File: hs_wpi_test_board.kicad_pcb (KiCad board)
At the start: 2 copper layers, 57.2 x 52.1 mm, 34 parts, among them J1 Raspberry_Pi_2_3, Q1 Q_NPN_EBC, Q10 Q_NPN_EBC, Q2 Q_NPN_EBC, Q3 Q_NPN_EBC, Q4 Q_NPN_EBC, Q5 Q_NPN_EBC, Q6 Q_NPN_EBC, Q7 Q_NPN_EBC, Q8 Q_NPN_EBC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

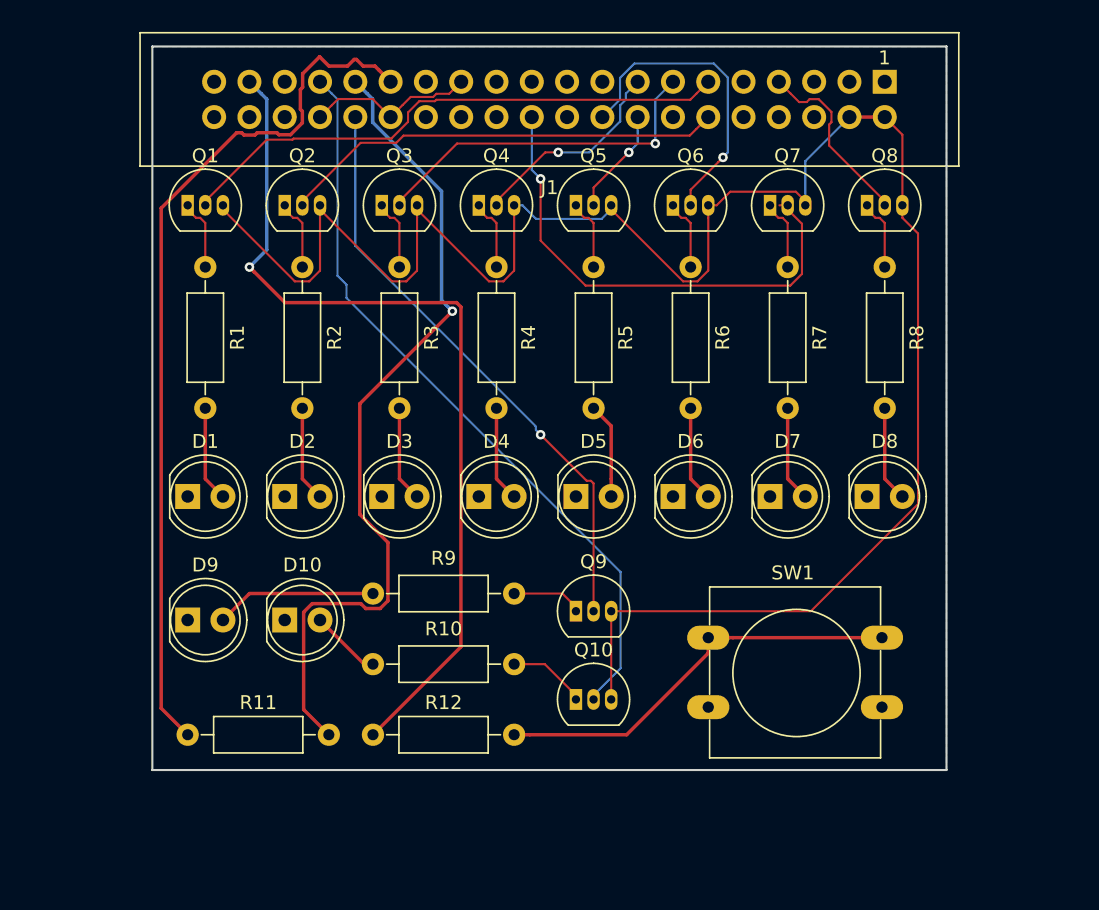
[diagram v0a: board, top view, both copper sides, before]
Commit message: remove all routing
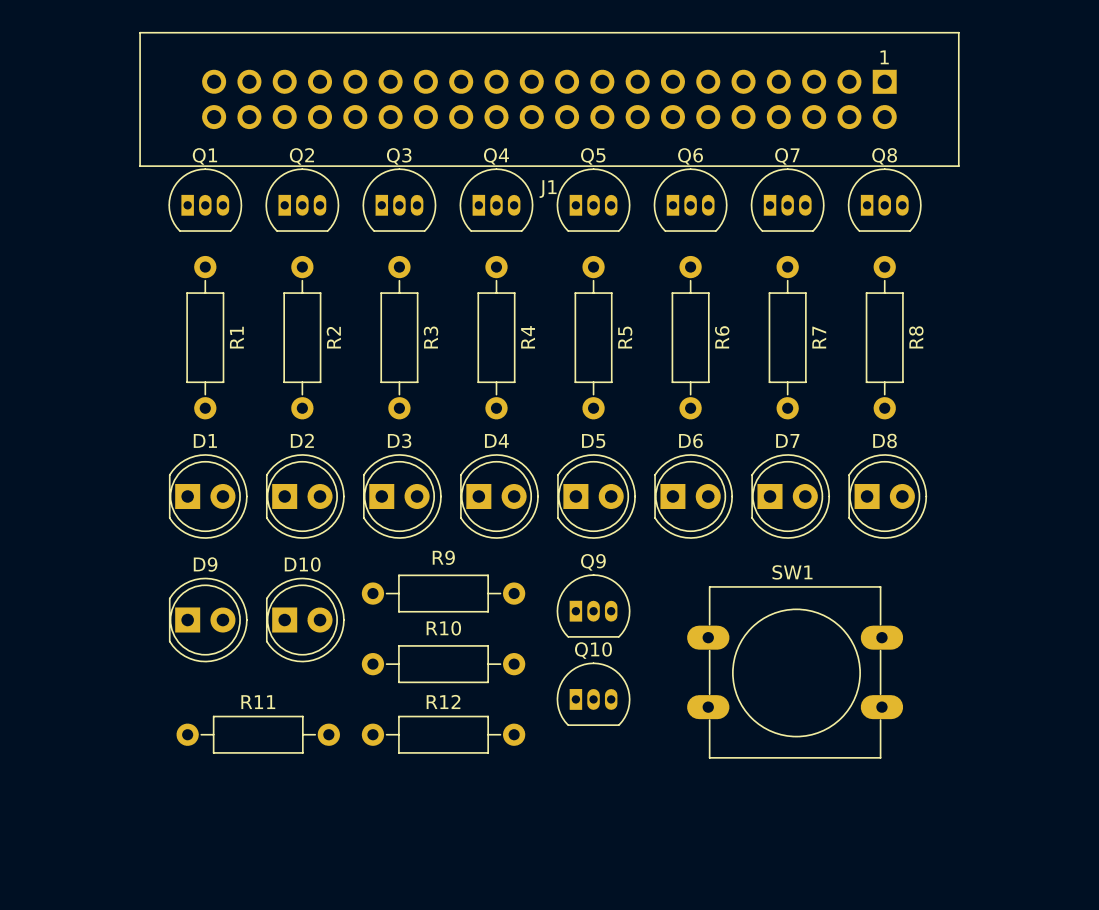
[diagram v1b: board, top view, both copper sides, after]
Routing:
- net VCC: track 144.4 -> 0.00 mm
- net /Button: track 64.2 -> 0.00 mm, vias 1 -> 0
- net Net-(J1-Pad29): track 63.3 -> 0.00 mm
- net Net-(J1-Pad31): track 60.1 -> 0.00 mm, vias 1 -> 0
- net /PWM1: track 54.2 -> 0.00 mm
- net /PWM0: track 42.8 -> 0.00 mm, vias 1 -> 0
- net /WPi0: track 40.4 -> 0.00 mm
- net /WPi6: track 35.6 -> 0.00 mm, vias 1 -> 0
- net /WPi1: track 32.0 -> 0.00 mm
- net Net-(R12-Pad2): track 30.0 -> 0.00 mm
- net /WPi2: track 25.4 -> 0.00 mm, vias 1 -> 0
- net /WPi5: track 22.2 -> 0.00 mm, vias 1 -> 0
- net /WPi3: track 15.0 -> 0.00 mm, vias 1 -> 0
- net /WPi7: track 13.3 -> 0.00 mm
- net GND: track 12.3 -> 0.00 mm
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- removed copper zone on B.Cu, net GND
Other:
- board outline removed

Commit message: switch to wider footprint for transistors
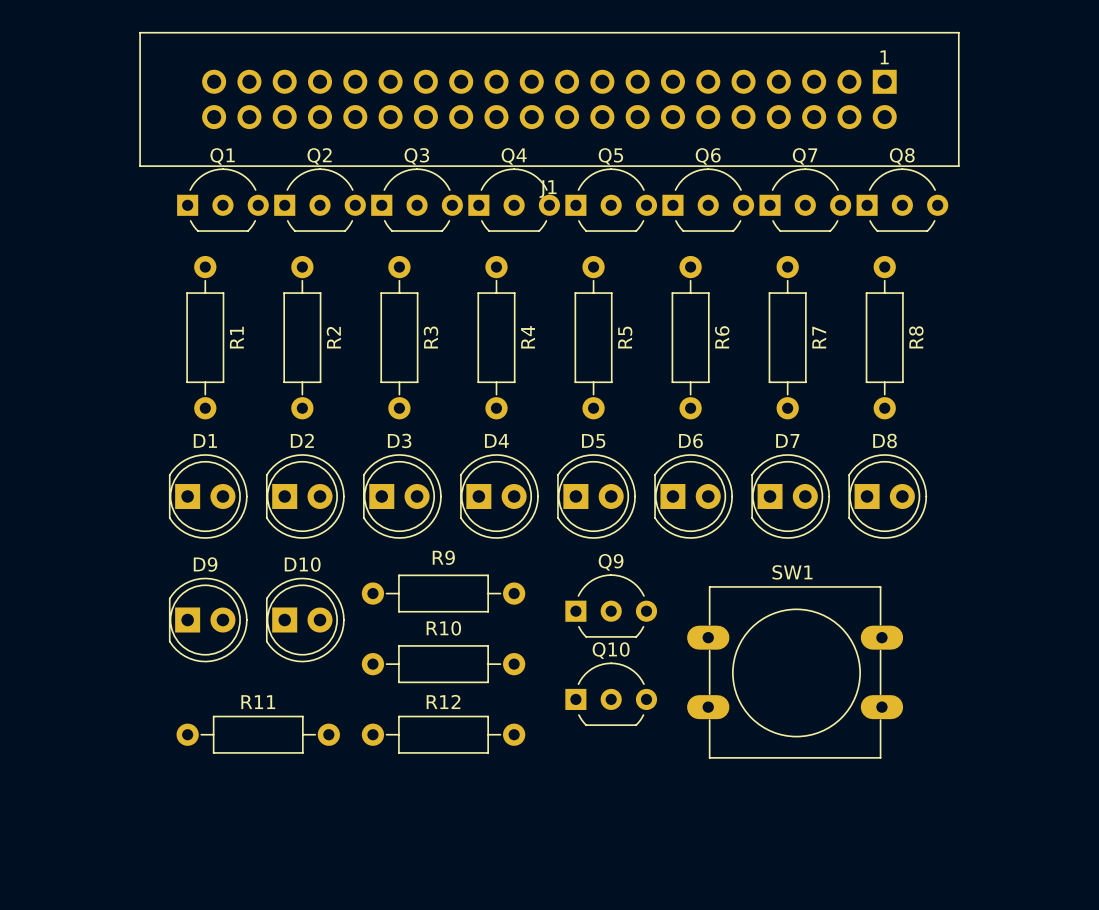
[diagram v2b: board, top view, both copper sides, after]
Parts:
- Q1, Q10, Q2, Q3, Q4, Q5, Q6, Q7, Q8, Q9: footprint TO_SOT_Packages_THT:TO-92_Inline_Narrow_Oval -> TO_SOT_Packages_THT:TO-92_Inline_Wide

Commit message: work in progress
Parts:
- moved R8 14.5 mm to (149.2, 103.5)
- moved R1 14.5 mm to (118.1, 103.5)
- moved R2 13.1 mm to (122.6, 103.5)
- moved R7 13.1 mm to (144.8, 103.5)
- moved R3 12.0 mm to (127.0, 103.5)
- moved R6 12.0 mm to (140.3, 103.5)
- moved R5 11.5 mm to (135.9, 103.5)
- moved R4 11.5 mm to (131.4, 103.5)
- moved D1 10.8 mm to (108.0, 97.8)
- moved D2 10.8 mm to (114.9, 97.8)
- moved D3 10.8 mm to (121.9, 97.8)
- moved D4 10.8 mm to (128.9, 97.8)
- moved D5 10.8 mm to (135.9, 97.8)
- moved D6 10.8 mm to (142.9, 97.8)
- moved D7 10.8 mm to (149.9, 97.8)
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
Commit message: position footprints
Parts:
- moved D10 56.6 mm to (163.8, 97.8)
- moved Q9 51.2 mm to (99.1, 90.2)
- moved Q10 50.0 mm to (163.2, 90.2)
- moved D9 29.4 mm to (101.0, 97.8)
- moved R10 29.3 mm to (158.1, 117.5)
- moved SW1 28.0 mm to (127.6, 106.0)
- moved R11 22.5 mm to (122.6, 117.5)
- moved R12 22.1 mm to (135.3, 117.5)
- moved R9 13.4 mm to (120.0, 117.5)
- moved R5 8.89 mm to (144.8, 103.5)
- moved R8 8.89 mm to (158.1, 103.5)
- moved R6 8.89 mm to (149.2, 103.5)
- moved R7 8.89 mm to (153.7, 103.5)
- moved R2 8.26 mm to (114.3, 103.5)
- moved R1 8.25 mm to (109.9, 103.5)
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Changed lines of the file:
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@@
   )
   (module LEDs:LED_D5.0mm (layer F.Cu)
-    (at 107.95 126.365)
+    (at 100.965 97.79)
     (descr "LED, diameter 5.0mm, 2 pins, http://cdn-reichelt.de/documents/datenblatt/A500/LL-504BC2E-009.pdf")
     (tags "LED diameter 5.0mm 2 pins")
@@
   )
   (module LEDs:LED_D5.0mm (layer F.Cu)
-    (at 114.935 126.365)
+    (at 163.83 97.79)
     (descr "LED, diameter 5.0mm, 2 pins, http://cdn-reichelt.de/documents/datenblatt/A500/LL-504BC2E-009.pdf")
     (tags "LED diameter 5.0mm 2 pins")
@@
   )
   (module Resistors_THT:R_Axial_DIN0207_L6.3mm_D2.5mm_P10.16mm_Horizontal (layer F.Cu)
-    (at 118.11 103.505 270)
+    (at 109.855 103.505 270)
     (descr "Resistor, Axial_DIN0207 series, Axial, Horizontal, pin pitch=10.16mm, 0.25W = 1/4W, length*diameter=6.3*2.5mm^2, http://cdn-reichelt.de/documents/datenblatt/B400/1_4W%23YAG.pdf")
     (tags "Resistor Axial_DIN0207 series Axial Horizontal pin pitch 10.16mm 0.25W = 1/4W length 6.3mm diameter 2.5mm")
@@
   )
   (module Resistors_THT:R_Axial_DIN0207_L6.3mm_D2.5mm_P10.16mm_Horizontal (layer F.Cu)
-    (at 122.555 103.505 270)
+    (at 114.3 103.505 270)
     (descr "Resistor, Axial_DIN0207 series, Axial, Horizontal, pin pitch=10.16mm, 0.25W = 1/4W, length*diameter=6.3*2.5mm^2, http://cdn-reichelt.de/documents/datenblatt/B400/1_4W%23YAG.pdf")
     (tags "Resistor Axial_DIN0207 series Axial Horizontal pin pitch 10.16mm 0.25W = 1/4W length 6.3mm diameter 2.5mm")
@@
   )
   (module Resistors_THT:R_Axial_DIN0207_L6.3mm_D2.5mm_P10.16mm_Horizontal (layer F.Cu)
-    (at 127 103.505 270)
+    (at 118.745 103.505 270)
     (descr "Resistor, Axial_DIN0207 series, Axial, Horizontal, pin pitch=10.16mm, 0.25W = 1/4W, length*diameter=6.3*2.5mm^2, http://cdn-reichelt.de/documents/datenblatt/B400/1_4W%23YAG.pdf")
     (tags "Resistor Axial_DIN0207 series Axial Horizontal pin pitch 10.16mm 0.25W = 1/4W length 6.3mm diameter 2.5mm")
@@
   )
   (module Resistors_THT:R_Axial_DIN0207_L6.3mm_D2.5mm_P10.16mm_Horizontal (layer F.Cu)
-    (at 131.445 103.505 270)
+    (at 123.19 103.505 270)
     (descr "Resistor, Axial_DIN0207 series, Axial, Horizontal, pin pitch=10.16mm, 0.25W = 1/4W, length*diameter=6.3*2.5mm^2, http://cdn-reichelt.de/documents/datenblatt/B400/1_4W%23YAG.pdf")
     (tags "Resistor Axial_DIN0207 series Axial Horizontal pin pitch 10.16mm 0.25W = 1/4W length 6.3mm diameter 2.5mm")
@@
   )
   (module Resistors_THT:R_Axial_DIN0207_L6.3mm_D2.5mm_P10.16mm_Horizontal (layer F.Cu)
-    (at 135.89 103.505 270)
+    (at 144.78 103.505 270)
     (descr "Resistor, Axial_DIN0207 series, Axial, Horizontal, pin pitch=10.16mm, 0.25W = 1/4W, length*diameter=6.3*2.5mm^2, http://cdn-reichelt.de/documents/datenblatt/B400/1_4W%23YAG.pdf")
     (tags "Resistor Axial_DIN0207 series Axial Horizontal pin pitch 10.16mm 0.25W = 1/4W length 6.3mm diameter 2.5mm")
@@
   )
   (module Resistors_THT:R_Axial_DIN0207_L6.3mm_D2.5mm_P10.16mm_Horizontal (layer F.Cu)
-    (at 140.335 103.505 270)
+    (at 149.225 103.505 270)
     (descr "Resistor, Axial_DIN0207 series, Axial, Horizontal, pin pitch=10.16mm, 0.25W = 1/4W, length*diameter=6.3*2.5mm^2, http://cdn-reichelt.de/documents/datenblatt/B400/1_4W%23YAG.pdf")
     (tags "Resistor Axial_DIN0207 series Axial Horizontal pin pitch 10.16mm 0.25W = 1/4W length 6.3mm diameter 2.5mm")
@@
   )
   (module Resistors_THT:R_Axial_DIN0207_L6.3mm_D2.5mm_P10.16mm_Horizontal (layer F.Cu)
-    (at 144.78 103.505 270)
+    (at 153.67 103.505 270)
     (descr "Resistor, Axial_DIN0207 series, Axial, Horizontal, pin pitch=10.16mm, 0.25W = 1/4W, length*diameter=6.3*2.5mm^2, http://cdn-reichelt.de/documents/datenblatt/B400/1_4W%23YAG.pdf")
     (tags "Resistor Axial_DIN0207 series Axial Horizontal pin pitch 10.16mm 0.25W = 1/4W length 6.3mm diameter 2.5mm")
@@
   )
   (module Resistors_THT:R_Axial_DIN0207_L6.3mm_D2.5mm_P10.16mm_Horizontal (layer F.Cu)
-    (at 149.225 103.505 270)
+    (at 158.115 103.505 270)
     (descr "Resistor, Axial_DIN0207 series, Axial, Horizontal, pin pitch=10.16mm, 0.25W = 1/4W, length*diameter=6.3*2.5mm^2, http://cdn-reichelt.de/documents/datenblatt/B400/1_4W%23YAG.pdf")
     (tags "Resistor Axial_DIN0207 series Axial Horizontal pin pitch 10.16mm 0.25W = 1/4W length 6.3mm diameter 2.5mm")
@@
   )
   (module Resistors_THT:R_Axial_DIN0207_L6.3mm_D2.5mm_P10.16mm_Horizontal (layer F.Cu)
-    (at 131.445 124.46 180)
+    (at 120.015 117.475 180)
     (descr "Resistor, Axial_DIN0207 series, Axial, Horizontal, pin pitch=10.16mm, 0.25W = 1/4W, length*diameter=6.3*2.5mm^2, http://cdn-reichelt.de/documents/datenblatt/B400/1_4W%23YAG.pdf")
     (tags "Resistor Axial_DIN0207 series Axial Horizontal pin pitch 10.16mm 0.25W = 1/4W length 6.3mm diameter 2.5mm")
@@
   )
   (module Resistors_THT:R_Axial_DIN0207_L6.3mm_D2.5mm_P10.16mm_Horizontal (layer F.Cu)
-    (at 131.445 129.54 180)
+    (at 158.115 117.475 180)
     (descr "Resistor, Axial_DIN0207 series, Axial, Horizontal, pin pitch=10.16mm, 0.25W = 1/4W, length*diameter=6.3*2.5mm^2, http://cdn-reichelt.de/documents/datenblatt/B400/1_4W%23YAG.pdf")
     (tags "Resistor Axial_DIN0207 series Axial Horizontal pin pitch 10.16mm 0.25W = 1/4W length 6.3mm diameter 2.5mm")
@@
   )
   (module Resistors_THT:R_Axial_DIN0207_L6.3mm_D2.5mm_P10.16mm_Horizontal (layer F.Cu)
-    (at 107.95 134.62)
+    (at 122.555 117.475)
     (descr "Resistor, Axial_DIN0207 series, Axial, Horizontal, pin pitch=10.16mm, 0.25W = 1/4W, length*diameter=6.3*2.5mm^2, http://cdn-reichelt.de/documents/datenblatt/B400/1_4W%23YAG.pdf")
     (tags "Resistor Axial_DIN0207 series Axial Horizontal pin pitch 10.16mm 0.25W = 1/4W length 6.3mm diameter 2.5mm")
@@
   )
   (module Resistors_THT:R_Axial_DIN0207_L6.3mm_D2.5mm_P10.16mm_Horizontal (layer F.Cu)
-    (at 121.285 134.62)
+    (at 135.255 117.475)
     (descr "Resistor, Axial_DIN0207 series, Axial, Horizontal, pin pitch=10.16mm, 0.25W = 1/4W, length*diameter=6.3*2.5mm^2, http://cdn-reichelt.de/documents/datenblatt/B400/1_4W%23YAG.pdf")
     (tags "Resistor Axial_DIN0207 series Axial Horizontal pin pitch 10.16mm 0.25W = 1/4W length 6.3mm diameter 2.5mm")
@@
   )
   (module Buttons_Switches_THT:SW_PUSH-12mm (layer F.Cu)
-    (at 145.415 127.635)
+    (at 127.635 106.045)
     (descr "SW PUSH 12mm https://www.e-switch.com/system/asset/product_line/data_sheet/143/TL1100.pdf")
     (tags "tact sw push 12mm")
@@
   )
   (module TO_SOT_Packages_THT:TO-92_Inline_Wide (layer F.Cu)
-    (at 135.89 125.73)
+    (at 99.06 90.17)
     (descr "TO-92 leads in-line, wide, drill 0.8mm (see NXP sot054_po.pdf)")
     (tags "to-92 sc-43 sc-43a sot54 PA33 transistor")
@@
   )
   (module TO_SOT_Packages_THT:TO-92_Inline_Wide (layer F.Cu)
-    (at 135.89 132.08)
+    (at 163.195 90.17)
     (descr "TO-92 leads in-line, wide, drill 0.8mm (see NXP sot054_po.pdf)")
     (tags "to-92 sc-43 sc-43a sot54 PA33 transistor")
@@
     )
   )
-  (gr_circle (center 165.735 121.92) (end 170.815 121.92) (layer B.SilkS) (width 1))
+  (gr_circle (center 165.735 113.665) (end 170.815 113.665) (layer B.SilkS) (width 1))
   (gr_circle (center 102.235 81.28) (end 107.315 81.28) (layer B.SilkS) (width 1))
-  (gr_circle (center 102.235 121.92) (end 107.315 121.92) (layer B.SilkS) (width 1))
+  (gr_circle (center 102.235 113.665) (end 107.315 113.665) (layer B.SilkS) (width 1))
   (gr_circle (center 165.735 81.28) (end 170.815 81.28) (layer B.SilkS) (width 1))
 )

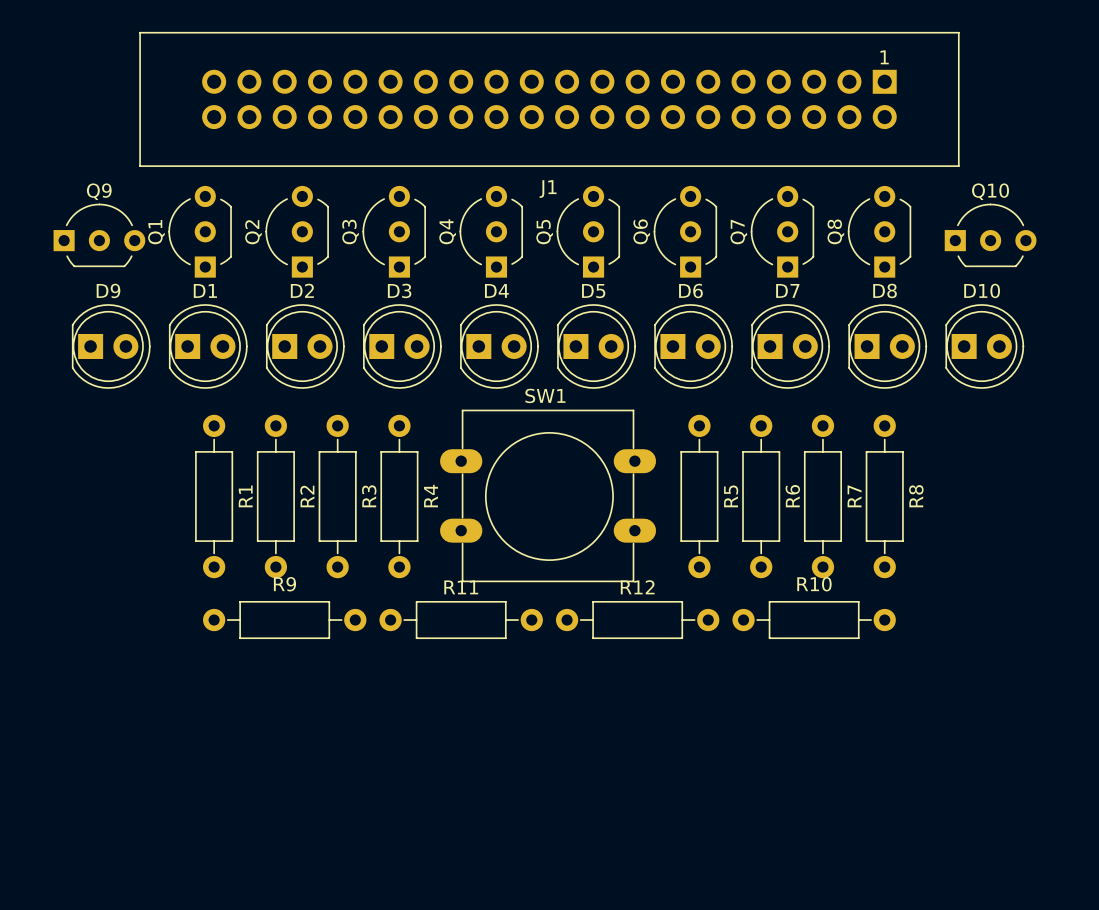
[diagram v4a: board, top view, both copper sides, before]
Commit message: draw board outline
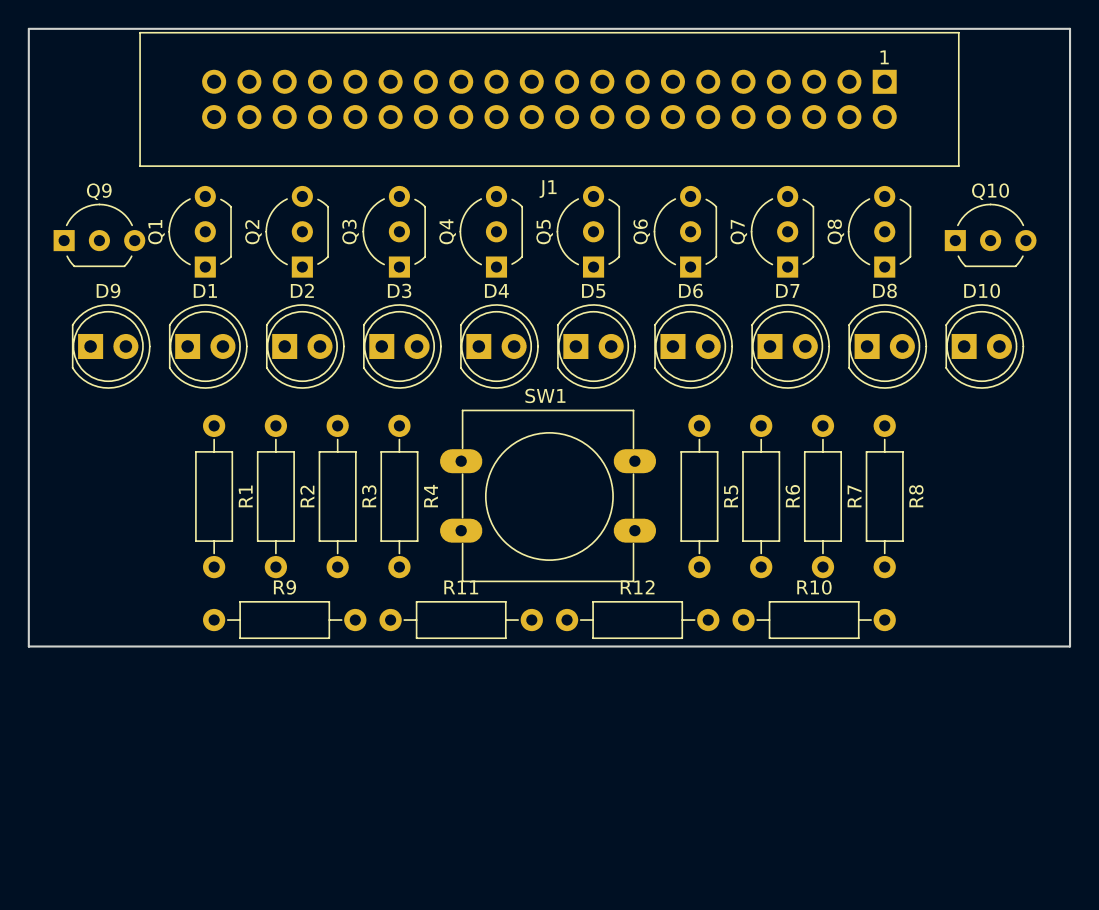
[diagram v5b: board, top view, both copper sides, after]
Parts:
- moved R10 10.2 mm to (148.0, 117.5), turned to 0 degrees
- moved R9 10.2 mm to (109.9, 117.5), turned to 0 degrees
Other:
- board outline added: 74.9 x 44.4 mm

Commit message: finish routing
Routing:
- net VCC: track 0.00 -> 75.7 mm
- net /Button: track 0.00 -> 71.5 mm
- net Net-(J1-Pad31): track 0.00 -> 63.7 mm, vias 0 -> 1
- net /WPi1: track 0.00 -> 58.7 mm, vias 0 -> 1
- net /PWM1: track 0.00 -> 57.8 mm
- net /WPi0: track 0.00 -> 53.8 mm, vias 0 -> 1
- net GND: track 0.00 -> 50.2 mm
- net Net-(J1-Pad29): track 0.00 -> 43.5 mm, vias 0 -> 3
- net Net-(Q10-Pad1): track 0.00 -> 38.3 mm
- net /WPi2: track 0.00 -> 32.3 mm, vias 0 -> 1
- net Net-(Q9-Pad1): track 0.00 -> 31.8 mm
- net Net-(D9-Pad2): track 0.00 -> 31.2 mm
- net Net-(R12-Pad2): track 0.00 -> 26.1 mm
- net Net-(D10-Pad2): track 0.00 -> 23.1 mm
- net /PWM0: track 0.00 -> 22.1 mm
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- added copper zone on B.Cu, net GND
